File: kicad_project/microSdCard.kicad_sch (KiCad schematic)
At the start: 5 parts, among them J1 Micro_SD_Card_Det_Hirose_DM3AT

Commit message: Pcb to production
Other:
- note added: "Micro SD"
- company: (none) -> HW Media Lab LLC
- title: (none) -> WebScreen Project
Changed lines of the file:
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@@
 	(generator_version "8.0")
 	(paper "A4")
+	(title_block
+		(title "WebScreen Project")
+		(date "2024-11-02")
+		(rev "1.2")
+		(company "HW Media Lab LLC")
+	)
 	(junction
 		(at 189.23 101.6)
@@
 		)
 	)
+	(text "Micro SD"
+		(exclude_from_sim no)
+		(at 241.046 27.432 0)
+		(effects
+			(font
+				(face "ISOCPEUR")
+				(size 7.62 7.62)
+				(thickness 0.254)
+				(bold yes)
+			)
+			(justify left bottom)
+		)
+	)
 	(hierarchical_label "SCK"
 		(shape input)
 		(at 199.39 101.6 0)
-		(fields_autoplaced yes)
 		(effects
 			(font
@@
 		(shape input)
 		(at 163.83 93.98 0)
-		(fields_autoplaced yes)
 		(effects
 			(font
@@
 		(shape input)
 		(at 199.39 106.68 0)
-		(fields_autoplaced yes)
 		(effects
 			(font
@@
 		(shape input)
 		(at 199.39 96.52 0)
-		(fields_autoplaced yes)
 		(effects
 			(font
@@
 			)
 		)
+		(property "Sim.Device" ""
+			(at 196.85 87.63 0)
+			(effects
+				(font
+					(size 1.27 1.27)
+				)
+				(hide yes)
+			)
+		)
+		(property "Sim.Pins" ""
+			(at 196.85 87.63 0)
+			(effects
+				(font
+					(size 1.27 1.27)
+				)
+				(hide yes)
+			)
+		)
 		(pin "1"
 		)
@@
 			)
 		)
+		(property "Sim.Device" ""
+			(at 181.61 87.63 0)
+			(effects
+				(font
+					(size 1.27 1.27)
+				)
+				(hide yes)
+			)
+		)
+		(property "Sim.Pins" ""
+			(at 181.61 87.63 0)
+			(effects
+				(font
+					(size 1.27 1.27)
+				)
+				(hide yes)
+			)
+		)
 		(pin "1"
 		)
@@
 			)
 		)
+		(property "Sim.Device" ""
+			(at 189.23 87.63 0)
+			(effects
+				(font
+					(size 1.27 1.27)
+				)
+				(hide yes)
+			)
+		)
+		(property "Sim.Pins" ""
+			(at 189.23 87.63 0)
+			(effects
+				(font
+					(size 1.27 1.27)
+				)
+				(hide yes)
+			)
+		)
 		(pin "1"
 		)
@@
 			)
 		)
+		(property "Sim.Device" ""
+			(at 208.28 100.33 0)
+			(effects
+				(font
+					(size 1.27 1.27)
+				)
+				(hide yes)
+			)
+		)
+		(property "Sim.Pins" ""
+			(at 208.28 100.33 0)
+			(effects
+				(font
+					(size 1.27 1.27)
+				)
+				(hide yes)
+			)
+		)
 		(pin "1"
 		)
@@
 			(at 137.16 101.6 0)
 			(effects
+				(font
+					(size 1.27 1.27)
+				)
+				(hide yes)
+			)
+		)
+		(property "Sim.Device" ""
+			(at 137.16 101.6 0)
+			(effects
+				(font
+					(size 1.27 1.27)
+				)
+				(hide yes)
+			)
+		)
+		(property "Sim.Pins" ""
+			(at 137.16 101.6 0)
+			(effects

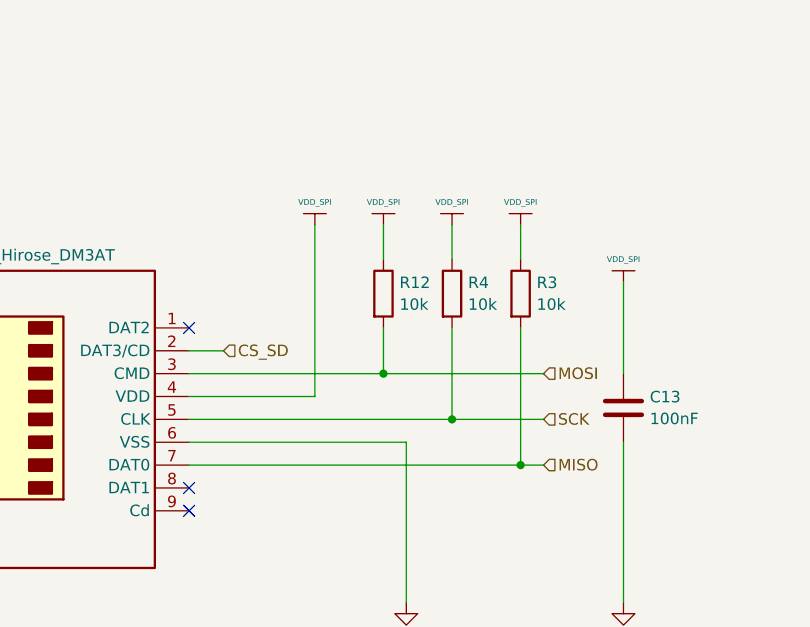
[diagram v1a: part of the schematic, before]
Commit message: Design revision: SD improvements, flash update, silkscreen and USB differential fix
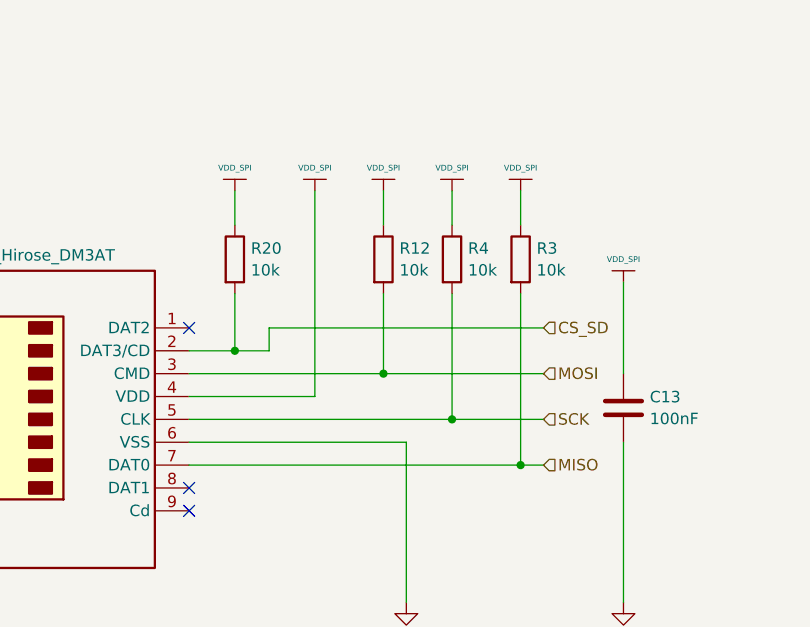
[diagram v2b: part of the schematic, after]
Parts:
- added R20: 10k, Resistor_SMD:R_0402_1005Metric, symbol Device:R
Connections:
- net CS_SD: now also R20.2
- net VDD_SPI: now also R20.1
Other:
- moved on the sheet: R12, R3, R4

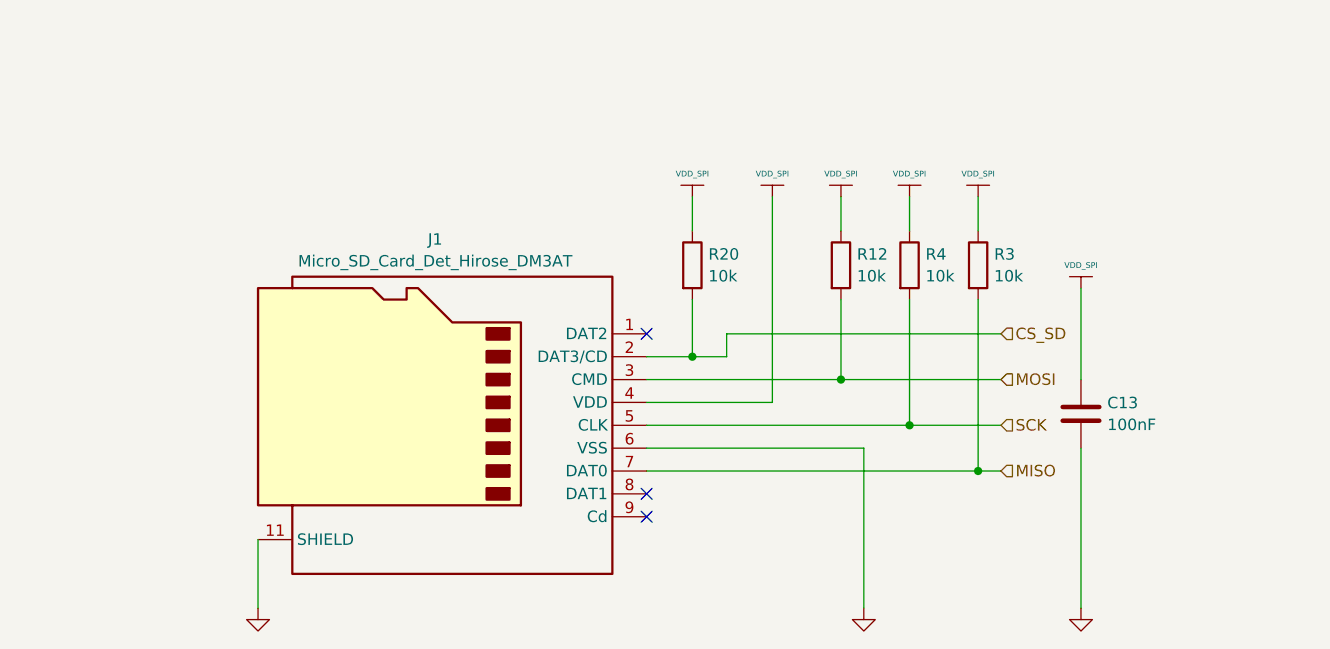
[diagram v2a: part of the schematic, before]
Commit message: Change SD card power source from VDD_SPI to 3V3 to support A1 cards
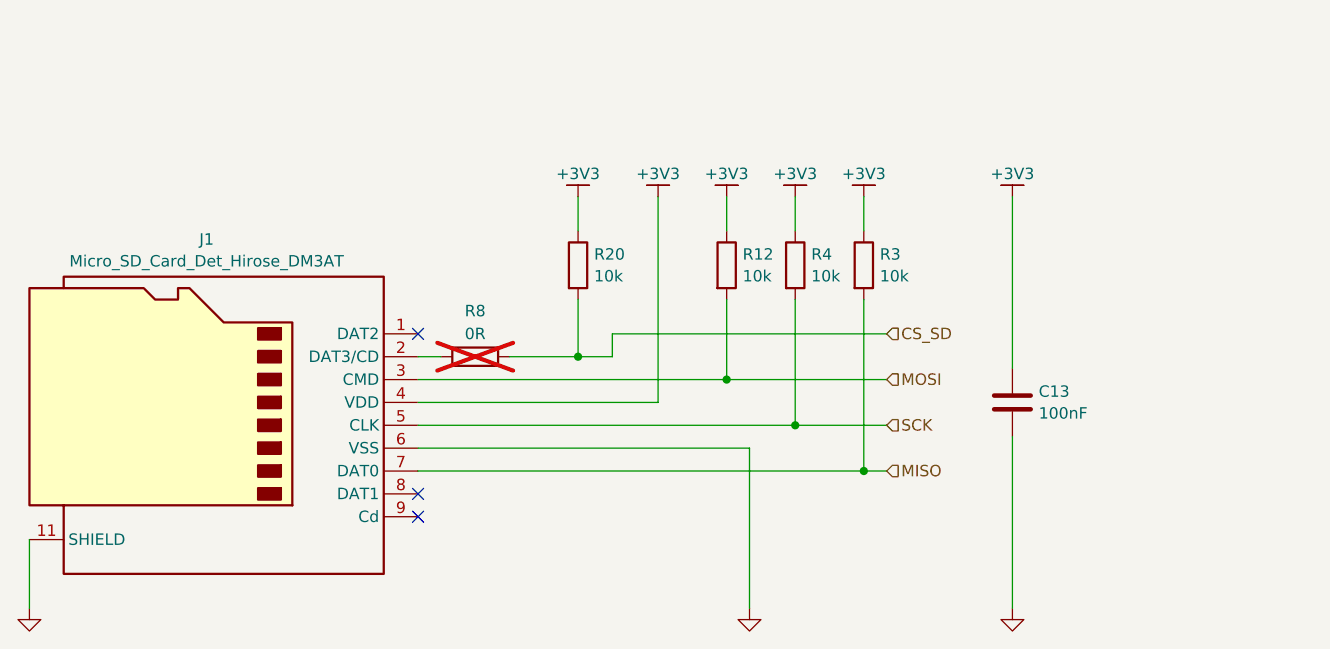
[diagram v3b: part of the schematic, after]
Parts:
- added R8: 0R, Resistor_SMD:R_0402_1005Metric, symbol Device:R
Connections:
- net CS_SD: now also R8.2; no longer J1.2 (DAT3/CD)
- net VDD_SPI renamed +3V3
- new net: J1.2 (DAT3/CD), R8.1
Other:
- moved on the sheet: C13, J1, R12, R20, R3, R4
